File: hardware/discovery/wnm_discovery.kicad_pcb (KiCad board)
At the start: 2 copper layers, 96.5 x 66 mm, 56 parts, among them J1 HEADER_2, J2 HEADER_25x2, J3 HEADER_25x2, J5 HEADER_2, SW1 SW_PUSH, SW10 SW_PUSH, SW11 SW_PUSH, SW12 SW_PUSH, SW13 SW_PUSH, SW14 SW_PUSH, SW15 SW_PUSH, SW16 SW_PUSH, SW17 SW_PUSH, SW18 SW_PUSH, SW19 SW_PUSH, SW2 SW_PUSH, SW20 SW_PUSH, SW21 SW_PUSH, SW22 SW_PUSH, SW3 SW_PUSH, SW4 SW_PUSH, SW5 SW_PUSH, SW6 SW_PUSH, SW7 SW_PUSH, SW8 SW_PUSH, SW9 SW_PUSH

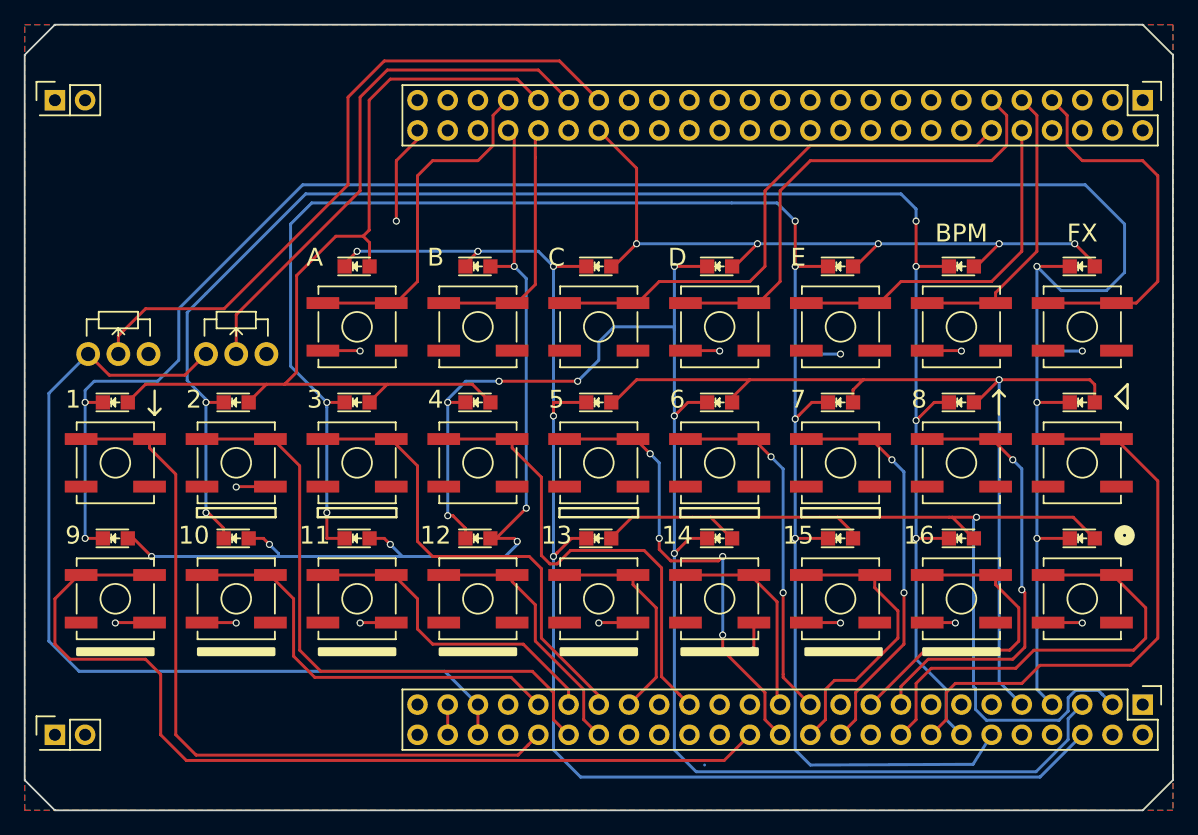
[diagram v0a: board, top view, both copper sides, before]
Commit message: HW: Update discovery with new UI design (encoders, screen, buttons layout)
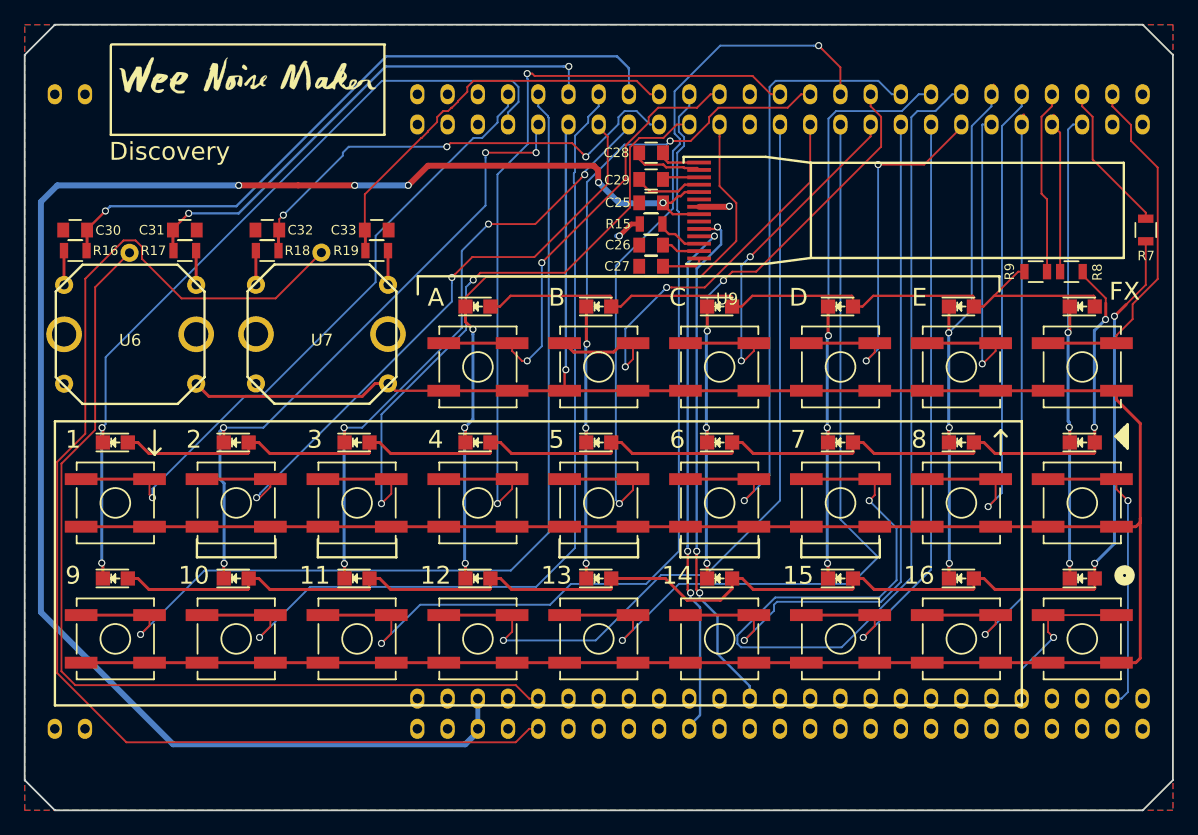
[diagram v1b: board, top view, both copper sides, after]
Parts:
- removed D19: LED, LEDs:LED_0805
- removed J1, J5: HEADER_2, Pin_Headers:Pin_Header_Straight_2x01
- removed J2, J3: HEADER_25x2, Pin_Headers:Pin_Header_Straight_2x25
- removed RV1, RV2: POT, Potentiometers:Potentiometer_WirePads_Small
- removed SW17: SW_PUSH, Buttons_Switches_SMD:SW_SPST_B3SL-1002P
- added C25: 10uF, Capacitors_SMD:C_0805, F.Cu at (132.7, 93.7)
- added C26: 10uF, Capacitors_SMD:C_0805, F.Cu at (132.7, 97.3)
- added C27: 10uF, Capacitors_SMD:C_0805, F.Cu at (132.7, 99.0)
- added C28: 1uF, Capacitors_SMD:C_0805, F.Cu at (132.7, 89.5)
- added C29: 1uF, Capacitors_SMD:C_0805, F.Cu at (132.7, 91.8)
- added C30: 0,1uF, Capacitors_SMD:C_0805, F.Cu at (84.3, 96.0)
- added C31: 0,1uF, Capacitors_SMD:C_0805, F.Cu at (93.5, 96.0)
- added C32: 0,1uF, Capacitors_SMD:C_0805, F.Cu at (100.4, 96.0)
- added C33: 0,1uF, Capacitors_SMD:C_0805, F.Cu at (109.6, 96.0)
- added G***: LOGO, POSS:logo_hand_line, F.Cu at (98.8, 86.2)
- added G***: LOGO, POSS:logo_hand_text, F.Cu at (98.8, 83.0)
- added R15: R, Resistors_SMD:R_0805, F.Cu at (132.7, 95.5)
- added R16: 27K, Resistors_SMD:R_0805, F.Cu at (84.3, 97.7)
- added R17: 27K, Resistors_SMD:R_0805, F.Cu at (93.5, 97.7)
- added R18: 27K, Resistors_SMD:R_0805, F.Cu at (100.4, 97.7)
- added R19: 27K, Resistors_SMD:R_0805, F.Cu at (109.6, 97.7)
- added R7: R, Resistors_SMD:R_0805, F.Cu at (174.2, 96.0)
- added R8: R, Resistors_SMD:R_0805, F.Cu at (168.0, 99.5)
- added R9: R, Resistors_SMD:R_0805, F.Cu at (165.0, 99.5)
- added U1: STM32F4_DISCO_Header, POSS:STM32F4-DISCO-HEADERS-TH, B.Cu at (80.0, 94.8)
- added U6: encoder_and_switch, POSS:encoder_EC12D, F.Cu at (88.9, 104.8)
- added U7: encoder_and_switch, POSS:encoder_EC12D, F.Cu at (105.0, 104.8)
- added U9: SSD1306, POSS:MIDAS_MCOT096016AV_OLED, F.Cu at (135.5, 98.8)
- moved D25 83.6 mm to (168.9, 102.4)
- moved D10 81.3 mm to (87.6, 113.9)
- moved D24 64.0 mm to (158.8, 102.4)
- moved D18 61.1 mm to (168.9, 113.9)
- moved D23 45.1 mm to (148.6, 102.4)
- moved D16 43.3 mm to (148.6, 113.9)
- moved D1 40.8 mm to (87.6, 125.3)
- moved D17 40.8 mm to (158.8, 113.9)
- moved D2 40.8 mm to (97.8, 125.3)
- moved D3 40.8 mm to (108.0, 125.3)
- moved D4 40.8 mm to (118.1, 125.3)
- moved D5 40.8 mm to (128.3, 125.3)
- moved D11 33.9 mm to (97.8, 113.9)
- moved D12 33.9 mm to (108.0, 113.9)
- moved D13 33.9 mm to (118.1, 113.9)
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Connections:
- net /GND renamed WAKEUP
- D1 pad 1: /PC9 -> COL1
- D1 pad 2: /COL1 -> Net-(D1-Pad2)
- D10 pad 1: /PA8 -> COL1
- D10 pad 2: /COL2 -> Net-(D10-Pad2)
- D11 pad 1: /PC9 -> COL2
- D11 pad 2: /COL3 -> Net-(D10-Pad2)
- D12 pad 1: /PC8 -> COL3
- D12 pad 2: /COL3 -> Net-(D10-Pad2)
- D13 pad 1: /PA15 -> COL4
- D13 pad 2: /COL3 -> Net-(D10-Pad2)
- D14 pad 1: /PC11 -> COL5
- D14 pad 2: /COL3 -> Net-(D10-Pad2)
- D15 pad 1: /PA8 -> COL6
- D15 pad 2: /COL3 -> Net-(D10-Pad2)
- D16 pad 1: /PC9 -> COL7
- D16 pad 2: /COL4 -> Net-(D10-Pad2)
- D17 pad 1: /PC8 -> COL8
- D17 pad 2: /COL4 -> Net-(D10-Pad2)
- D18 pad 1: /PA15 -> COL9
- D18 pad 2: /COL4 -> Net-(D10-Pad2)
- D2 pad 1: /PC8 -> COL2
- D2 pad 2: /COL1 -> Net-(D1-Pad2)
- D20 pad 1: /PA8 -> COL4
- D20 pad 2: /COL4 -> Net-(D20-Pad2)
- D21 pad 1: /PC9 -> COL5
- D21 pad 2: /COL5 -> Net-(D20-Pad2)
- D22 pad 1: /PC8 -> COL6
- D22 pad 2: /COL5 -> Net-(D20-Pad2)
- D23 pad 1: /PA15 -> COL7
- D23 pad 2: /COL5 -> Net-(D20-Pad2)
- D24 pad 1: /PC11 -> COL8
- D24 pad 2: /COL5 -> Net-(D20-Pad2)
- D25 pad 1: /PA8 -> COL9
- D25 pad 2: /COL5 -> Net-(D20-Pad2)
- D3 pad 1: /PA15 -> COL3
- D3 pad 2: /COL1 -> Net-(D1-Pad2)
- D4 pad 1: /PC11 -> COL4
- D4 pad 2: /COL1 -> Net-(D1-Pad2)
- D5 pad 1: /PA8 -> COL5
- D5 pad 2: /COL1 -> Net-(D1-Pad2)
- D6 pad 1: /PC9 -> COL6
- D6 pad 2: /COL2 -> Net-(D1-Pad2)
- D7 pad 1: /PC8 -> COL7
- D7 pad 2: /COL2 -> Net-(D1-Pad2)
- D8 pad 1: /PA15 -> COL8
- D8 pad 2: /COL2 -> Net-(D1-Pad2)
- D9 pad 1: /PC11 -> COL9
- D9 pad 2: /COL2 -> Net-(D1-Pad2)
- Play1 pad 1: /PD0 -> Play
- Play2 pad 1: /FX -> FX
- SW1 pad 1: /B1 -> B1
- SW10 pad 1: /B10 -> B10
- SW11 pad 1: /B11 -> B11
- SW12 pad 1: /B12 -> B12
- SW13 pad 1: /B13 -> B13
- SW14 pad 1: /B14 -> B14
- SW15 pad 1: /B15 -> B15
- SW16 pad 1: /B16 -> B16
- SW18 pad 1: /BF2 -> BA
- SW19 pad 1: /BF3 -> BB
- SW2 pad 1: /B2 -> B2
- SW20 pad 1: /BF4 -> BC
- SW21 pad 1: /BF5 -> BD
- SW22 pad 1: /BPM -> BE
- SW3 pad 1: /B3 -> B3
- SW4 pad 1: /B4 -> B4
- SW5 pad 1: /B5 -> B5
- SW6 pad 1: /B6 -> B6
- SW7 pad 1: /B7 -> B7
- SW8 pad 1: /B8 -> B8
- SW9 pad 1: /B9 -> B9
- Write1 pad 1: /PD2 -> Write
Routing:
- net WAKEUP: track 42.0 -> 303.9 mm, vias 13 -> 1
- net /PA8: track 172.4 -> 0.00 mm, vias 5 -> 0
- net /PA15: track 146.8 -> 0.00 mm, vias 6 -> 0
- net /PC11: track 142.5 -> 0.00 mm, vias 6 -> 0
- net 3V3: track 0.00 -> 141.9 mm, vias 0 -> 5
- net /PC8: track 125.1 -> 0.00 mm, vias 7 -> 0
- net Net-(D1-Pad2): track 0.00 -> 122.3 mm, vias 0 -> 2
- net /PC9: track 118.0 -> 0.00 mm, vias 5 -> 0
- net Net-(D10-Pad2): track 0.00 -> 107.0 mm, vias 0 -> 2
- net ENC_2_SW: track 0.00 -> 102.8 mm
- net B7: track 0.00 -> 92.3 mm, vias 0 -> 1
- net B9: track 0.00 -> 82.8 mm, vias 0 -> 1
- net /COL4: track 82.7 -> 0.00 mm
- net /COL5: track 82.0 -> 0.00 mm, vias 6 -> 0
- net /COL1: track 80.0 -> 0.00 mm, vias 1 -> 0
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- added copper zone on B.Cu, net GND
- added copper zone on F.Cu, net GND
- removed copper zone on B.Cu, net WAKEUP
- removed copper zone on F.Cu, net WAKEUP
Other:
- net class DAC_traces added: clearance 0.16, trace_width 0.16, via_dia 0.6, via_drill 0.4
- net class power added: clearance 0.3, trace_width 0.5, via_dia 0.6, via_drill 0.4
- rule pad_to_mask_clearance: 0.2 -> 0.08
- rule trace_min: 0.2 -> 0.16
- board text added: "Discovery"
- board text added: "OUT"
- board text removed: "BPM"

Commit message: HW: Use a different MCU pins for the discovery board
This simplifies the PCB layout.
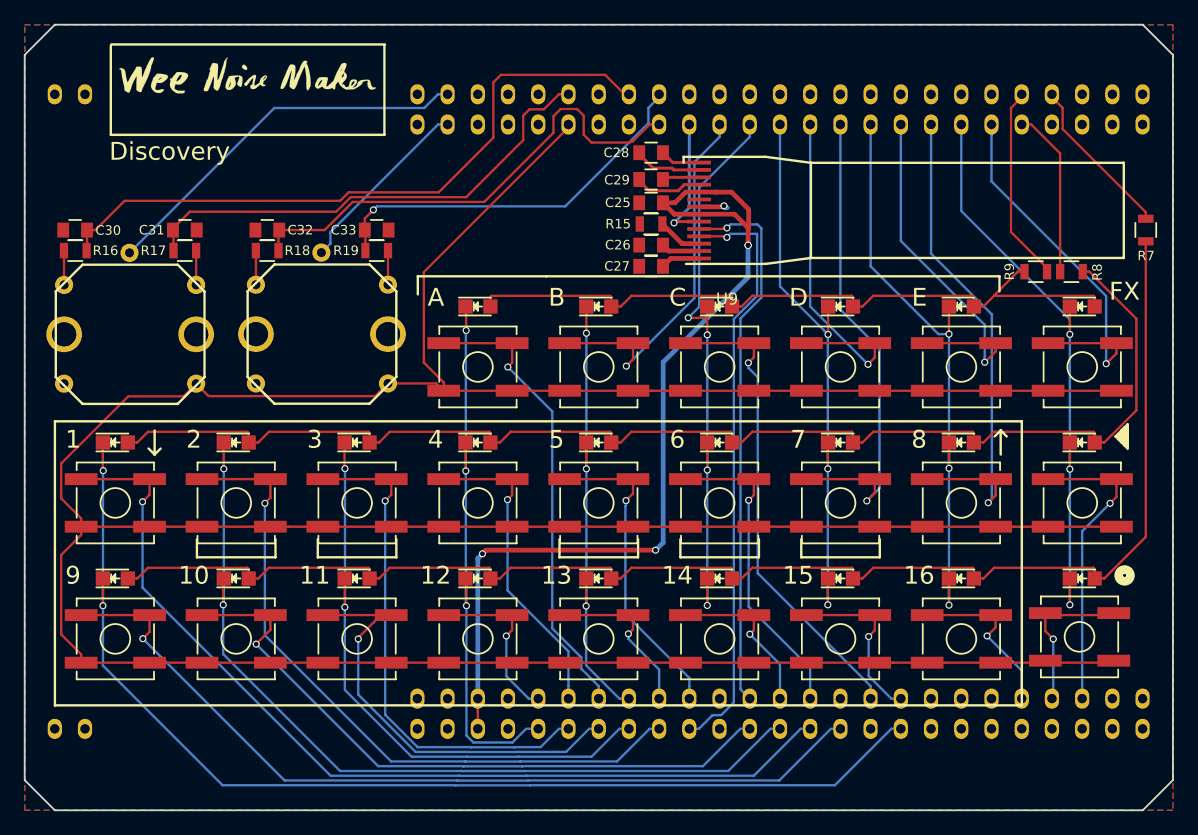
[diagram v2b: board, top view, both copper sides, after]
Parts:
- moved Write1 0.28 mm to (168.7, 130.2)
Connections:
- U1 pad 100: (no net) -> SWDIO
- U1 pad 101: (no net) -> VBUS
- U1 pad 102: (no net) -> Net-(U1-Pad102)
- U1 pad 103: (no net) -> I2S_MCLK
- U1 pad 12: B11 -> Net-(U1-Pad12)
- U1 pad 13: BA -> Net-(U1-Pad13)
- U1 pad 14: (no net) -> Net-(U1-Pad14)
- U1 pad 15: B4 -> Net-(U1-Pad15)
- U1 pad 16: COL5 -> Net-(U1-Pad16)
- U1 pad 17: B5 -> Net-(U1-Pad17)
- U1 pad 18: COL6 -> Net-(U1-Pad18)
- U1 pad 19: B6 -> Net-(U1-Pad19)
- U1 pad 20: COL7 -> Net-(U1-Pad20)
- U1 pad 21: B7 -> Net-(U1-Pad21)
- U1 pad 22: COL8 -> Net-(U1-Pad22)
- U1 pad 23: B8 -> ROW3
- U1 pad 24: ROW3 -> ROW1
- U1 pad 25: ROW1 -> STM_LED2
- U1 pad 26: FX -> STM_LED4
- U1 pad 29: (no net) -> ENC_2_SW
- U1 pad 30: (no net) -> Net-(U1-Pad30)
- U1 pad 31: COL1 -> Net-(U1-Pad31)
- U1 pad 32: COL2 -> Net-(U1-Pad32)
- U1 pad 34: B2 -> Net-(U1-Pad34)
- U1 pad 35: COL3 -> I2S_LRCLK
- U1 pad 37: B3 -> Screen_NReset
- U1 pad 38: COL4 -> BB
- U1 pad 39: (no net) -> COL6
- U1 pad 4: (no net) -> ENC_1_SW
- U1 pad 40: B12 -> COL7
- U1 pad 41: BB -> BD
- U1 pad 42: B13 -> B7
- U1 pad 43: BC -> COL8
- U1 pad 44: B14 -> BE
- U1 pad 45: B15 -> B8
- U1 pad 46: BD -> COL9
- U1 pad 47: BE -> FX
- U1 pad 48: B16 -> ROW2
- U1 pad 49: ROW2 -> STM_LED1
- U1 pad 5: (no net) -> Net-(U1-Pad5)
- U1 pad 50: COL9 -> STM_LED3
- U1 pad 51: (no net) -> Net-(U1-Pad51)
- U1 pad 56: (no net) -> Net-(U1-Pad56)
- U1 pad 58: (no net) -> Net-(U1-Pad58)
- U1 pad 59: ENC_1_SW -> B12
- U1 pad 6: B1 -> Net-(U1-Pad6)
- U1 pad 60: (no net) -> B4
- U1 pad 61: (no net) -> BA
- U1 pad 62: (no net) -> COL5
- U1 pad 63: (no net) -> B13
- U1 pad 64: (no net) -> B5
- U1 pad 65: (no net) -> Net-(U1-Pad65)
- U1 pad 67: (no net) -> B14
- U1 pad 68: (no net) -> B6
- U1 pad 69: (no net) -> USB_Over_Current
- U1 pad 7: B9 -> Net-(U1-Pad7)
- U1 pad 70: (no net) -> BC
- U1 pad 71: (no net) -> B15
- U1 pad 72: (no net) -> I2S_DIN
- U1 pad 73: (no net) -> I2S_SCLK
- U1 pad 74: (no net) -> SWCLK
- U1 pad 75: Write -> B16
- U1 pad 76: (no net) -> Write
- U1 pad 77: (no net) -> Play
- U1 pad 78: Play -> Net-(U1-Pad78)
- U1 pad 81: (no net) -> Net-(U1-Pad81)
- U1 pad 83: (no net) -> Net-(U1-Pad83)
- U1 pad 84: ENC_2_SW -> COL4
- U1 pad 85: (no net) -> B3
- U1 pad 86: (no net) -> B11
- U1 pad 87: (no net) -> COL3
- U1 pad 88: (no net) -> B2
- U1 pad 9: B10 -> Net-(U1-Pad9)
- U1 pad 90: (no net) -> Net-(U1-Pad90)
- U1 pad 91: (no net) -> B10
- U1 pad 92: (no net) -> COL2
- U1 pad 93: (no net) -> B1
- U1 pad 94: (no net) -> B9
- U1 pad 95: (no net) -> Audio_Reset
- U1 pad 96: (no net) -> COL1
- U1 pad 97: (no net) -> Net-(U1-Pad97)
- U1 pad 98: (no net) -> Net-(U1-Pad98)
- U1 pad 99: (no net) -> Net-(U1-Pad99)
- U9 pad 6: (no net) -> Net-(U9-Pad6)
- U9 pad 9: (no net) -> Screen_NReset
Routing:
- net ENC_2_SW: track 102.8 -> 15.6 mm
- net 3V3: track 141.9 -> 78.0 mm, vias 5 -> 4
- net B13: track 70.3 -> 14.0 mm
- net B12: track 67.9 -> 14.6 mm
- net B7: track 92.3 -> 41.3 mm
- net B14: track 62.2 -> 14.0 mm
- net ENC_1_SW: track 78.6 -> 32.3 mm
- net B4: track 68.2 -> 26.5 mm, vias 2 -> 1
- net B15: track 53.5 -> 14.6 mm
- net B11: track 75.9 -> 37.1 mm
- net B16: track 52.3 -> 14.3 mm
- net B5: track 64.4 -> 26.7 mm, vias 2 -> 1
- net B6: track 56.0 -> 26.5 mm
- net COL1: track 68.1 -> 94.3 mm
- net B1: track 54.9 -> 79.4 mm
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
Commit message: HW:Update revision of the discovery board
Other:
- board text added: "Rev-B"
- board text removed: "OUT"
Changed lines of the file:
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@@
   (general
     (links 199)
-    (no_connects 1)
+    (no_connects 0)
     (area 79.934999 78.664999 176.605001 144.855001)
     (thickness 1.6)
@@
   (module POSS:STM32F4-DISCO-HEADERS-TH (layer B.Cu)
     (at 80 94.75 270)
-    (fp_text reference U1 (at 0 -0.5 270) (layer B.SilkS)
+    (fp_text reference U1 (at 0 -0.5 270) (layer B.SilkS) hide
       (effects (font (size 1 1) (thickness 0.15)) (justify mirror))
     )
@@
       (xy -0.436719 -0.819846) (xy -0.381897 -0.886333) (xy -0.312891 -0.899472) (xy -0.228417 -0.859165)) (layer F.SilkS) (width 0.01))
   )
-  (gr_text "Discovery\n" (at 92.2 89.4) (layer F.SilkS)
+  (gr_text Rev-B (at 169.7482 141.5034) (layer B.SilkS)
+    (effects (font (size 1.5 1.5) (thickness 0.3)) (justify mirror))
+  )
+  (gr_text "Discovery\n" (at 92.2274 89.408) (layer F.SilkS)
     (effects (font (size 1.5 1.5) (thickness 0.3)))
   )
@@
     (arrow2b (pts (xy 80.01 73.66) (xy 81.136504 73.073579)))
   )
-  (gr_text OUT (at 170.25 99.75) (layer B.SilkS)
-    (effects (font (size 1.5 1.5) (thickness 0.3)) (justify mirror))
-  )
   (gr_line (start 81.28 143.51) (end 81.28 80.01) (angle 90) (layer Margin) (width 0.2))
